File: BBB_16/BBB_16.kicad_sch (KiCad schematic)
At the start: 40 parts, among them J17 Power In Left, J18 Power In Right, J19 GPIO, J23 VIN Voltage, J24 Expansion Header, J25 RTC Conn, J26 OLED, J27 Aux Pwr, J28 VIN Select, SW1 Left BTN, SW2 Up BTN, SW3 Down BTN, SW4 Right BTN, SW5 PWR BTN, U2 LM7805, U6 24L256

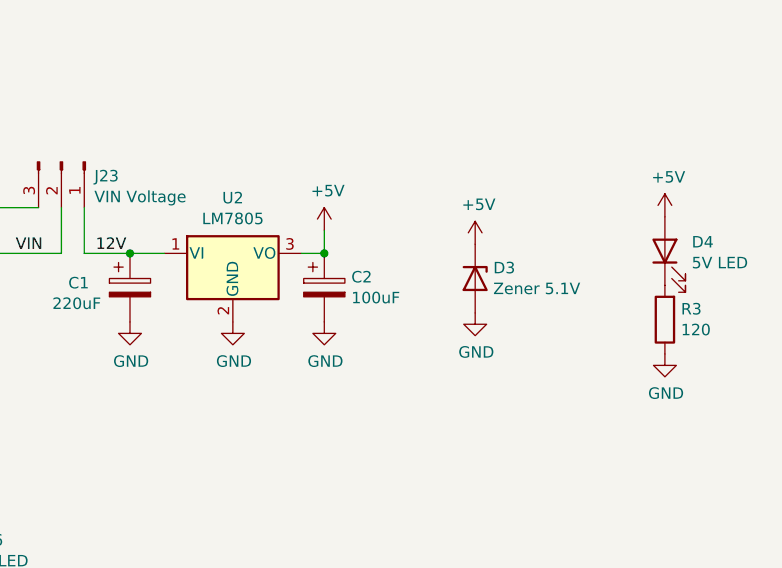
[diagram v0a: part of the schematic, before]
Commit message: added universal 5v to BBB16
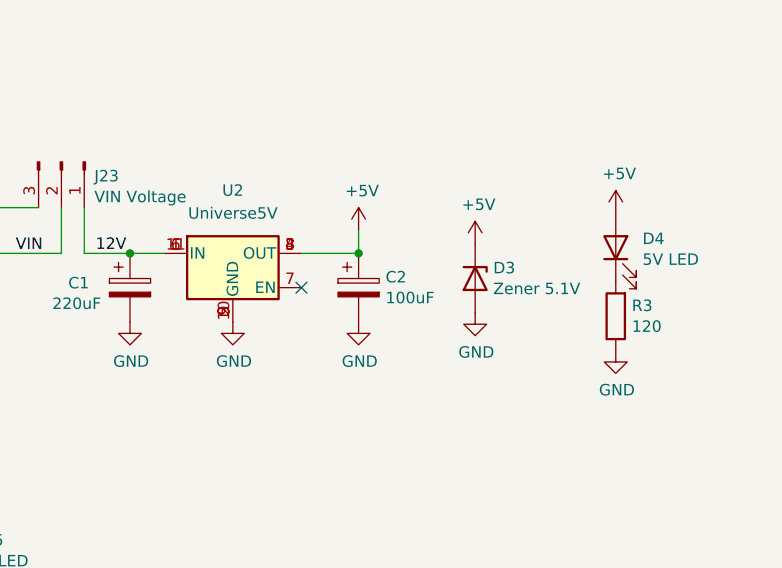
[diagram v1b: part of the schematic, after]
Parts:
- removed U2: LM7805, Package_TO_SOT_THT:TO-220-3_Vertical, symbol Regulator_Linear:LM7805_TO220
- added U2: Universe5V, Scotts:Universal_5V_Horizontal, symbol Scotts:Universe5V
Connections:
- net +5V: now also U2.3 (OUT), U2.4 (OUT), U2.8 (OUT)
- net 12V: now also U2.1 (IN), U2.11 (IN), U2.6 (IN)
- net GND: now also U2.10 (GND), U2.2 (GND), U2.5 (GND), U2.9 (GND)
- no-connect marks 1 -> 2
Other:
- moved on the sheet: C2, D4, R3

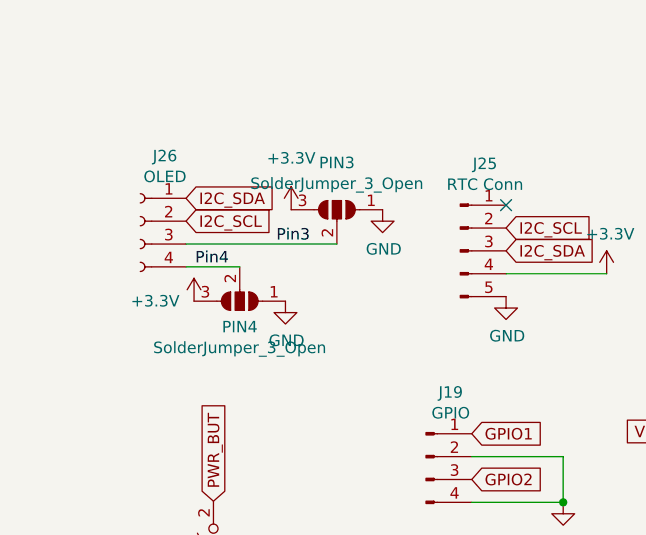
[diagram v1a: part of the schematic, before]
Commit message: added cut trace to OLED power pins
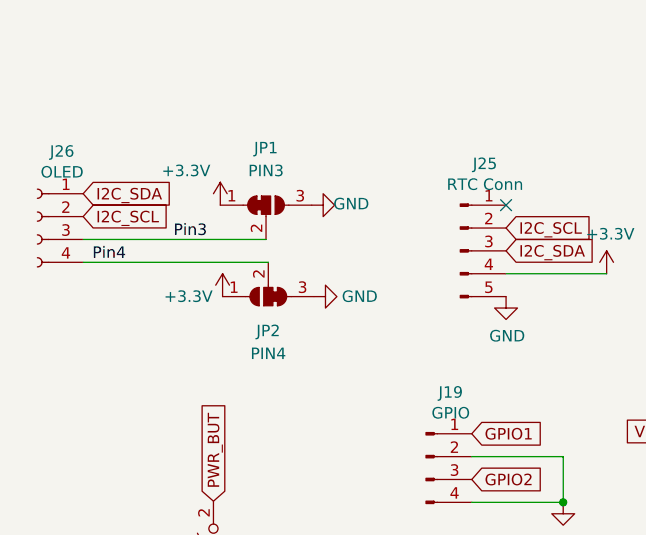
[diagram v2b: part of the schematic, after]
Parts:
- removed PIN3, PIN4: SolderJumper_3_Open, Jumper:SolderJumper-3_P1.3mm_Open_Pad1.0x1.5mm, symbol Jumper:SolderJumper_3_Open
- added JP1: PIN3, Scotts:SolderJumper-3_P1mm_Bridged12, symbol Jumper:SolderJumper_3_Bridged12
- added JP2: PIN4, Scotts:SolderJumper-3_P1mm_Bridged23, symbol Scotts:SolderJumper_3_Bridged23
- F17, F18: footprint Keystone_Fuse:FUSE_3544-2 -> Scotts:FUSE_3544-2
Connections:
- net +3V3: now also JP1.1 (A), JP2.1 (A)
- net GND: now also JP1.3 (B), JP2.3 (B)
- net Pin3: now also JP1.2 (C)
- net Pin4: now also JP2.2 (C)
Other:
- moved on the sheet: J26

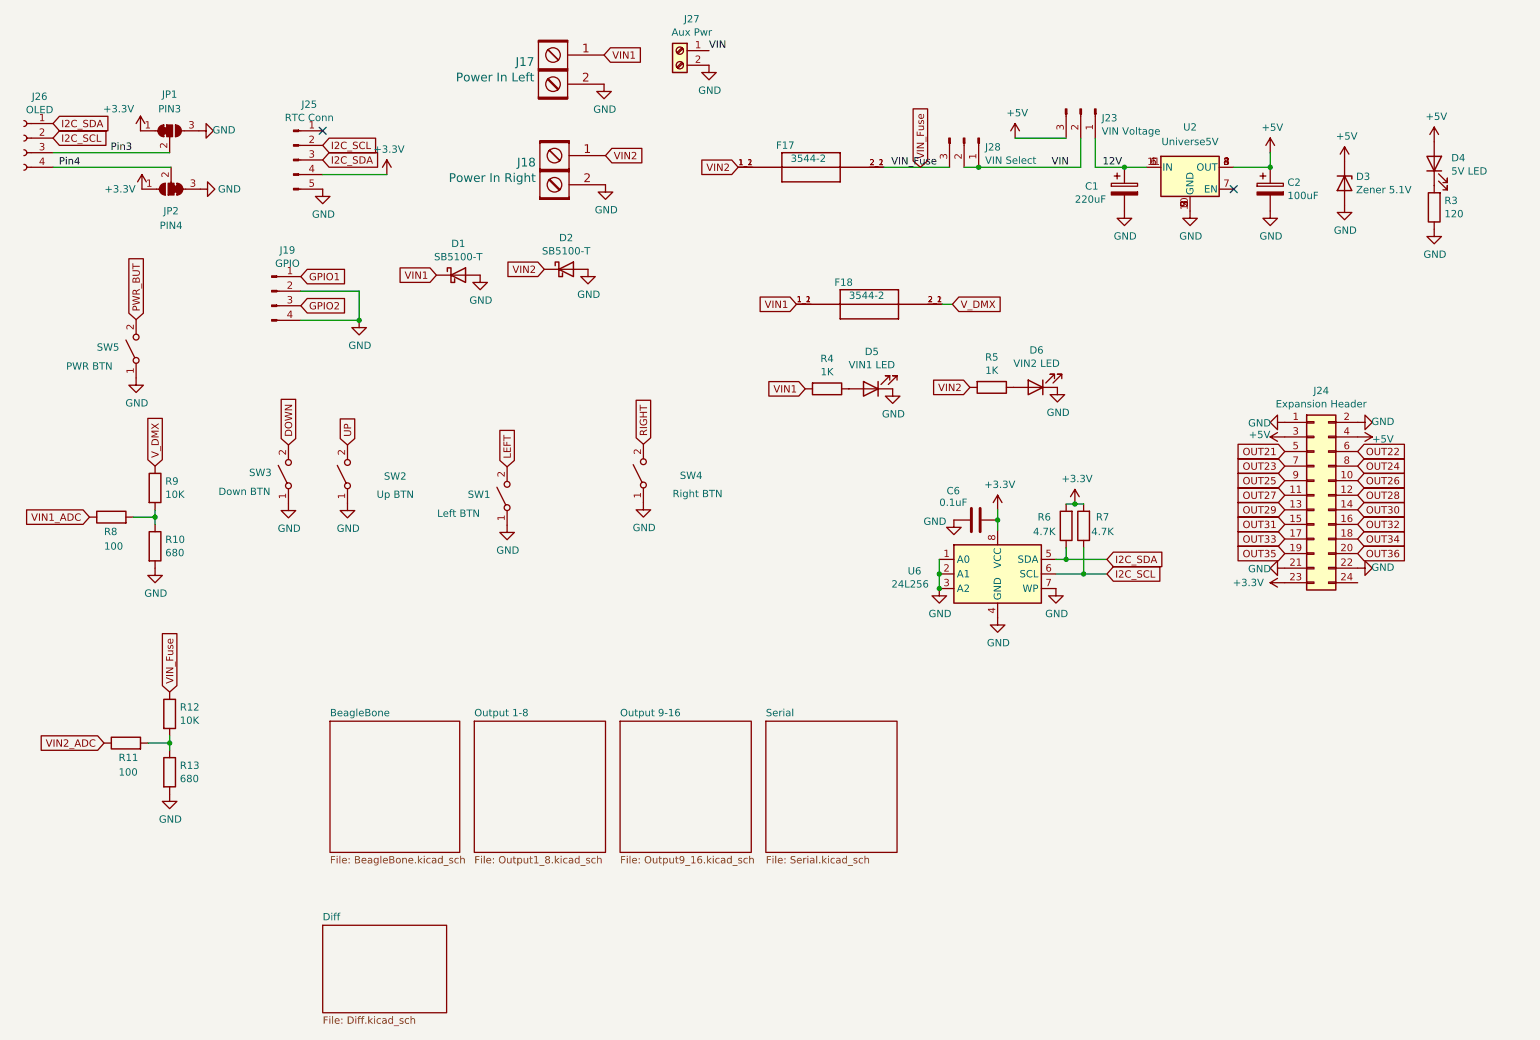
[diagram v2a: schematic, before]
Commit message: update to kicad v9
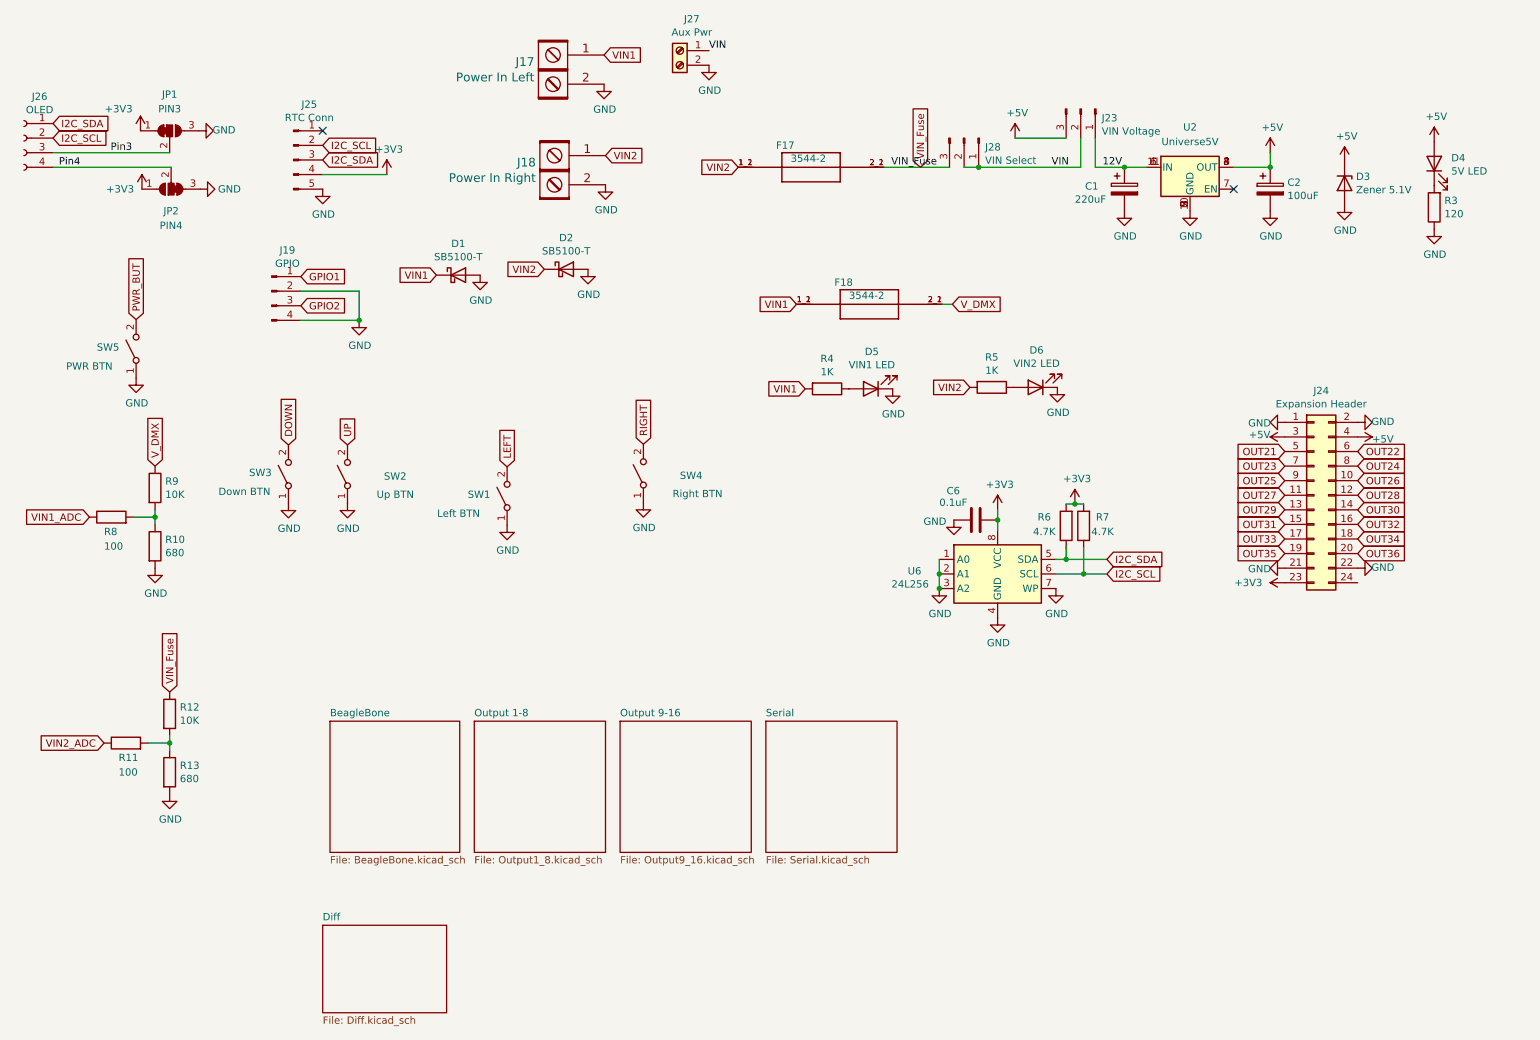
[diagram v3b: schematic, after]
